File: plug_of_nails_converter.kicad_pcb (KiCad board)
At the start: 2 copper layers, 44.8 x 31.7 mm, 6 parts, among them CN1 5103308-1

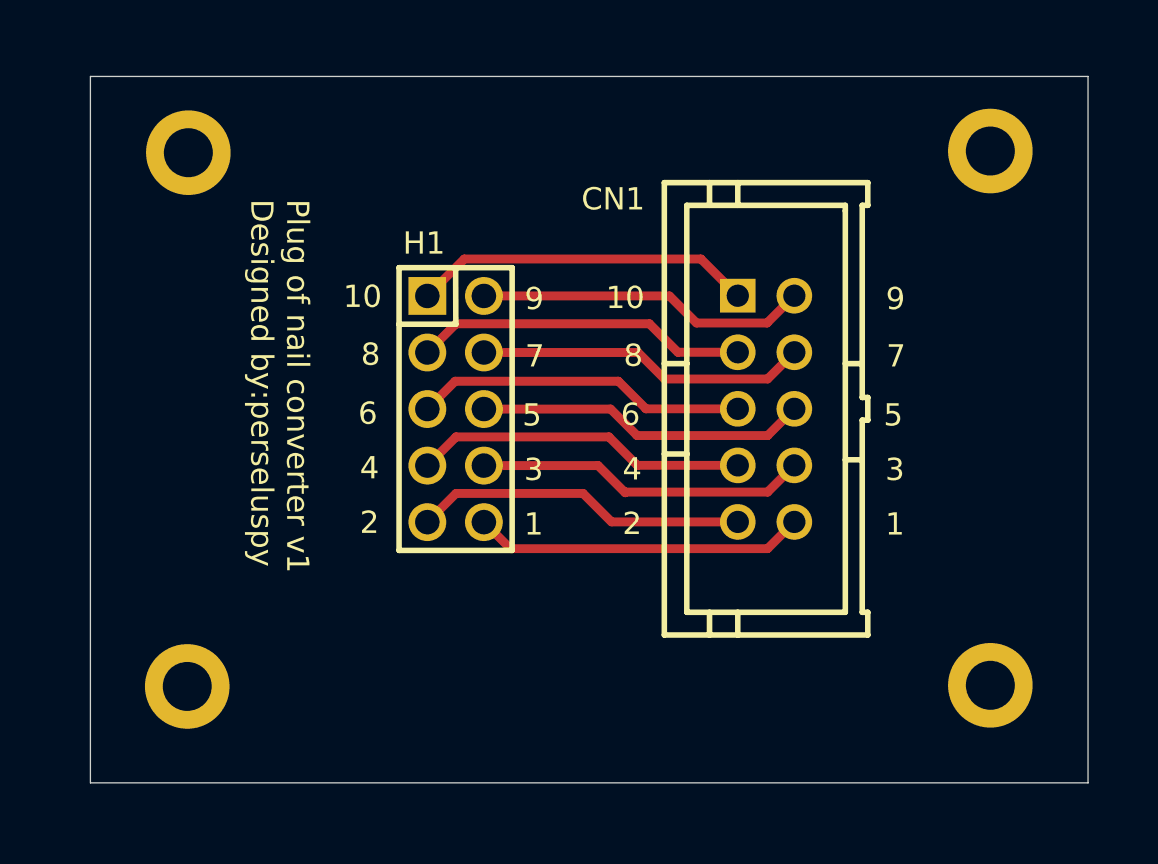
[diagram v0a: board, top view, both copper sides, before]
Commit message: Chaning IDC pin numbers and adding bottom CU layer
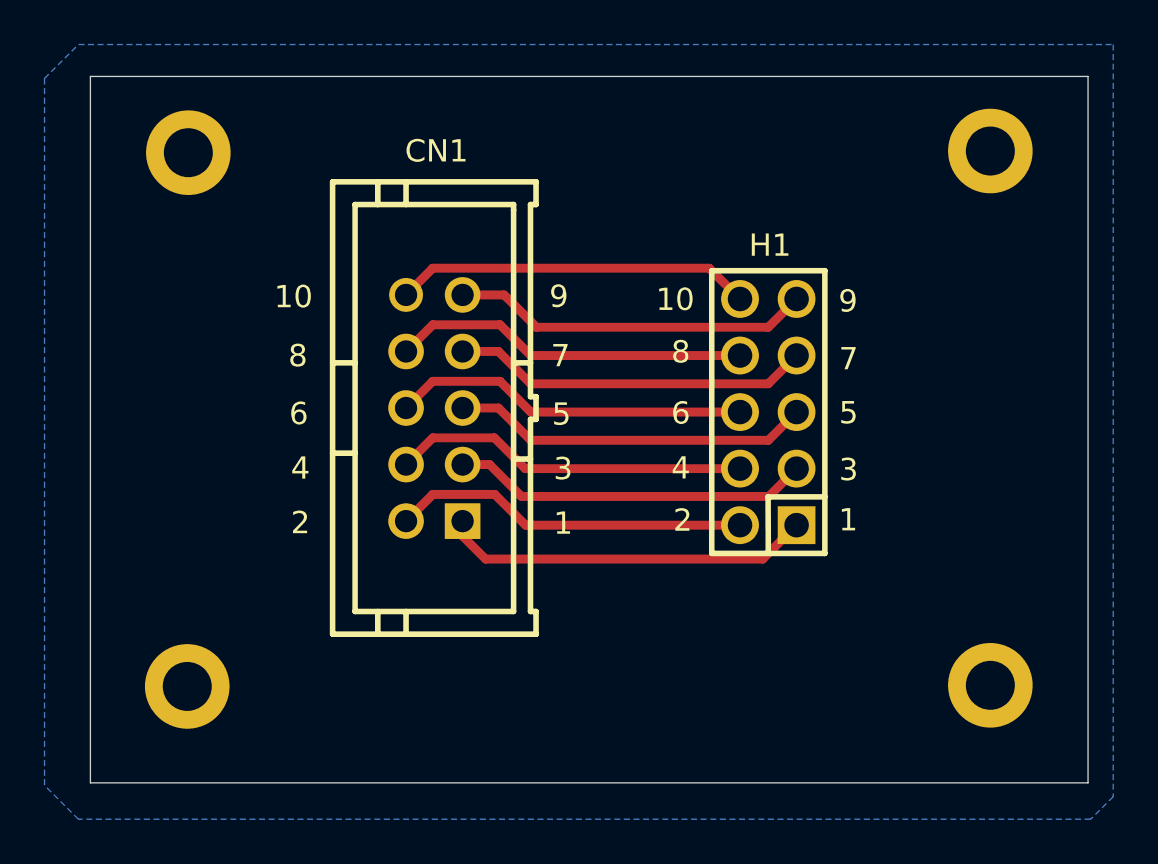
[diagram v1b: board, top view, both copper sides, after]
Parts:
- CN1: footprint my_lib:[10P_2X5_IDC_MALE]TE Connectivity 5103308-1 -> pepy_sym_lib:[10P_2X5_IDC_MALE]TE Connectivity 5103308-1
- H1: footprint my_lib:[10P_HEADER_STR]Ckmtw(Shenzhen Cankemeng) B-2100S10P-B110 -> pepy_sym_lib:[10P_HEADER_STR]Ckmtw(Shenzhen Cankemeng) B-2100S10P-B110
- H2, H3, H4, H5: footprint MountingHole:MountingHole_2.2mm_M2_DIN965_Pad -> pepy_sym_lib:[MOUNTING_HOLE]MountingHole_2.2mm_M2_DIN965_Pad
- moved CN1 14.9 mm to (123.2, 68.1)
- moved H1 14.0 mm to (138.2, 68.3), turned to 90 degrees
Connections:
- H2 pad 1: GND -> unconnected-(H2-Pad1)
- H3 pad 1: GND -> unconnected-(H3-Pad1)
- H4 pad 1: GND -> unconnected-(H4-Pad1)
- H5 pad 1: GND -> unconnected-(H5-Pad1)
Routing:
- net /P1: track 15.3 -> 17.4 mm
- net /P5: track 15.0 -> 16.1 mm
- net /P10: track 14.9 -> 16.1 mm
- net /P6: track 14.9 -> 16.1 mm
- net /P4: track 14.9 -> 16.1 mm
- net /P8: track 15.0 -> 16.1 mm
- net /P9: track 15.0 -> 16.1 mm
- net /P7: track 15.0 -> 16.1 mm
- net /P2: track 15.0 -> 16.1 mm
- net /P3: track 15.0 -> 16.1 mm
- added copper zone on B.Cu, net (none)
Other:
- board text added: "Plug of nails converter v2 perseluspy"
- board text removed: "Plug of nail converter v1 Designed by:perseluspy"

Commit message: Updating symbols and testing kibot
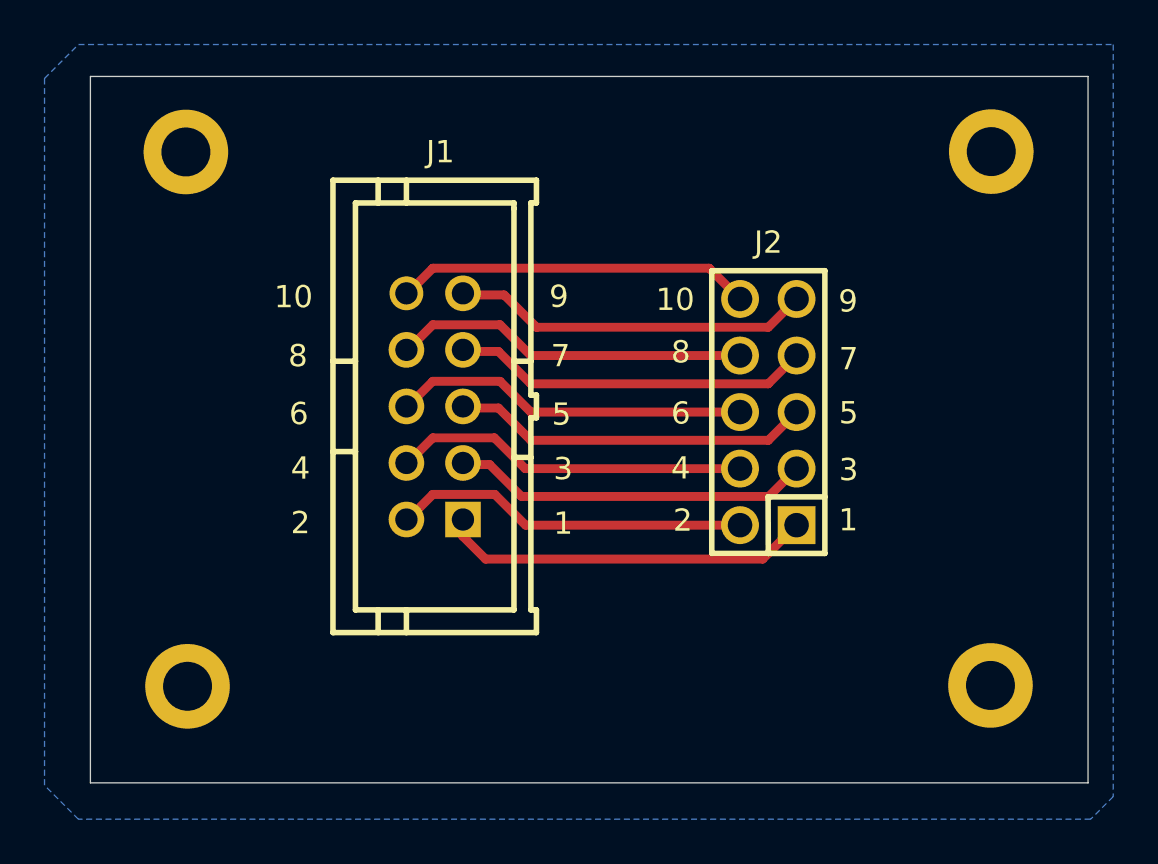
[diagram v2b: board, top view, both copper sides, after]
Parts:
- removed CN1: 5103308-1, pepy_sym_lib:[10P_2X5_IDC_MALE]TE Connectivity 5103308-1
- removed H1: 210S-2*5P L=11.6MMGold-plated black, pepy_sym_lib:[10P_HEADER_STR]Ckmtw(Shenzhen Cankemeng) B-2100S10P-B110
- removed H2, H3, H4, H5: MountingHole_Pad, pepy_sym_lib:[MOUNTING_HOLE]MountingHole_2.2mm_M2_DIN965_Pad
- added J1: 5103308-1, pepy_sym_lib:[10P_2X5_IDC_MALE]TE Connectivity 5103308-1, F.Cu at (123.2, 68.1)
- added J2: B-2100S10P-B110, pepy_sym_lib:[10P_HEADER_STR]Ckmtw(Shenzhen Cankemeng) B-2100S10P-B110, F.Cu at (138.2, 68.3)
- added MH1: MountingHole_Pad, pepy_sym_lib:[MOUNTING_HOLE]MountingHole_2.2mm_M2_DIN965_Pad, F.Cu at (112.0, 56.6)
- added MH2: MountingHole_Pad, pepy_sym_lib:[MOUNTING_HOLE]MountingHole_2.2mm_M2_DIN965_Pad, F.Cu at (148.2, 56.6)
- added MH3: MountingHole_Pad, pepy_sym_lib:[MOUNTING_HOLE]MountingHole_2.2mm_M2_DIN965_Pad, F.Cu at (148.2, 80.6)
- added MH4: MountingHole_Pad, pepy_sym_lib:[MOUNTING_HOLE]MountingHole_2.2mm_M2_DIN965_Pad, F.Cu at (112.1, 80.6)
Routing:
- net /P1: track 17.4 -> 16.7 mm
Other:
- board text added: "Plug of nails converter v2, perseluspy"
- board text removed: "Plug of nails converter v2 perseluspy"
